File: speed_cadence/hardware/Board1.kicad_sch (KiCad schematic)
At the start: 10 parts, among them IC1 AH1912-W-7, J1 DX07S016JA3R1500, SW1 SW_Push, U1 STM32F042G6U6TR, U2 TS2940CW33_RPG

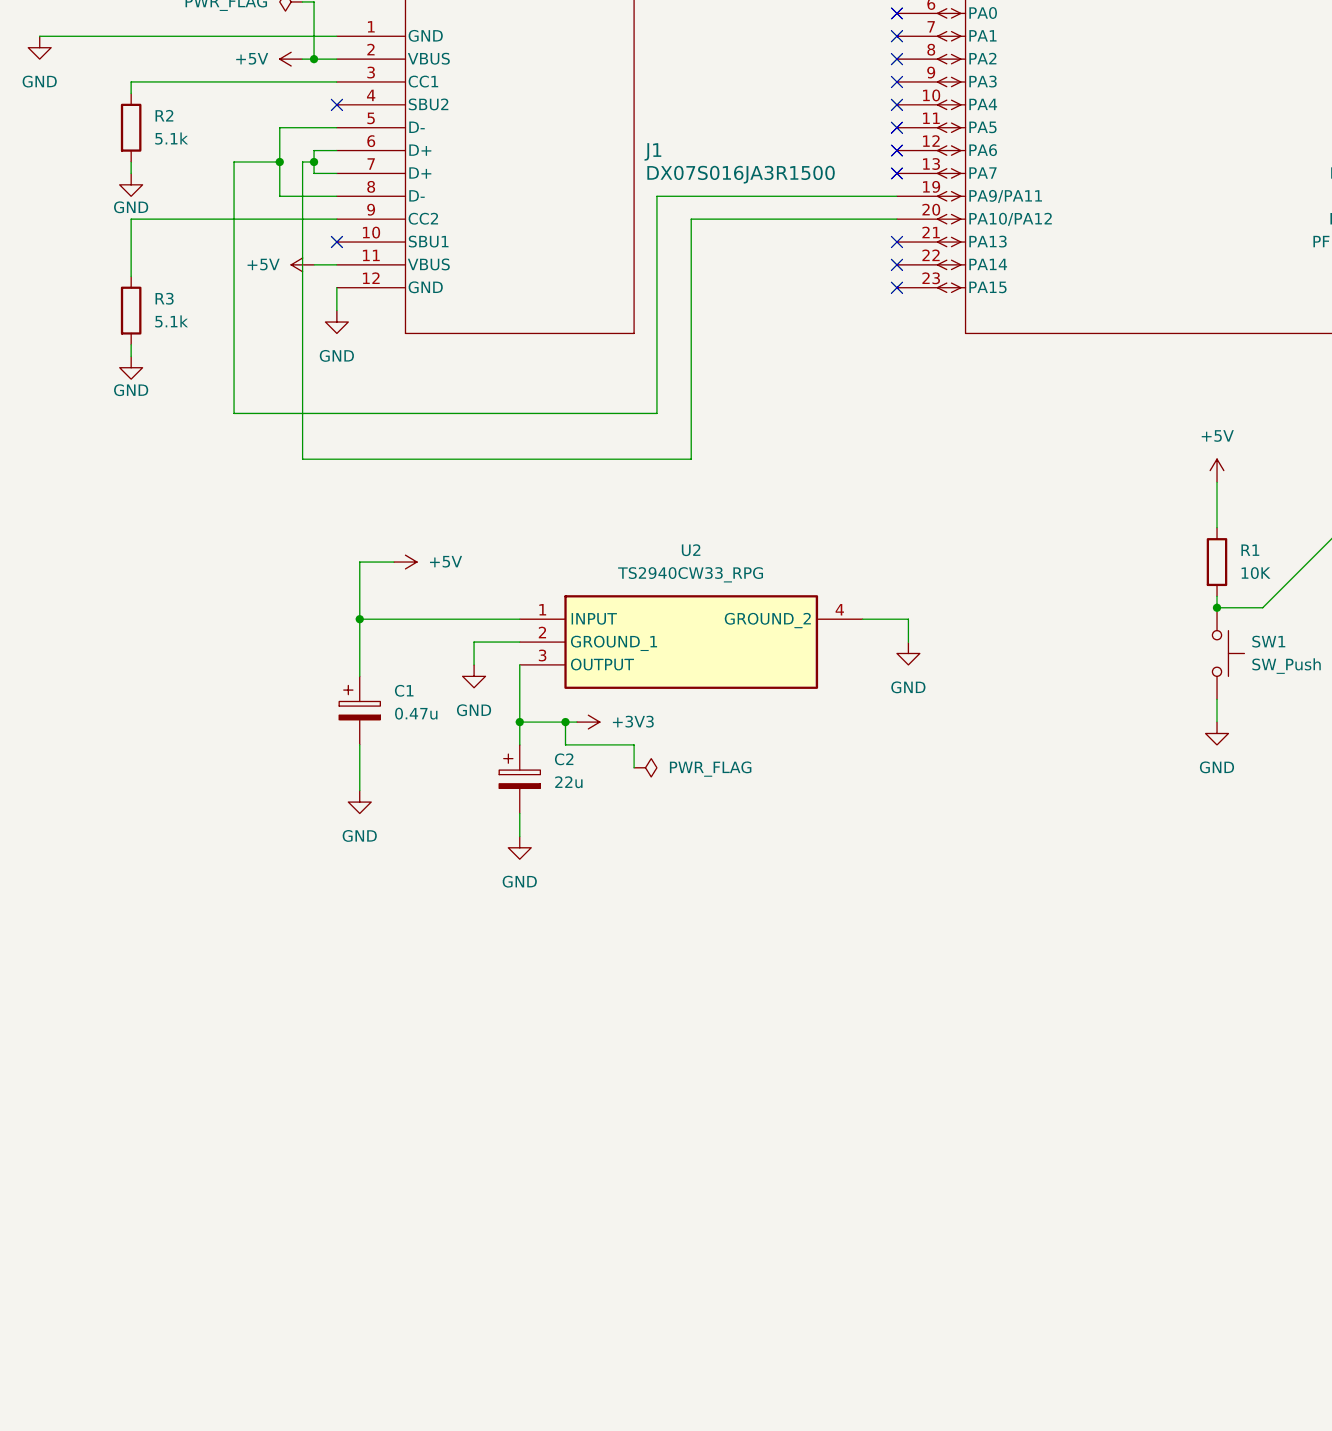
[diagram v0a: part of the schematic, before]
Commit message: Added final pins and finished physical layout
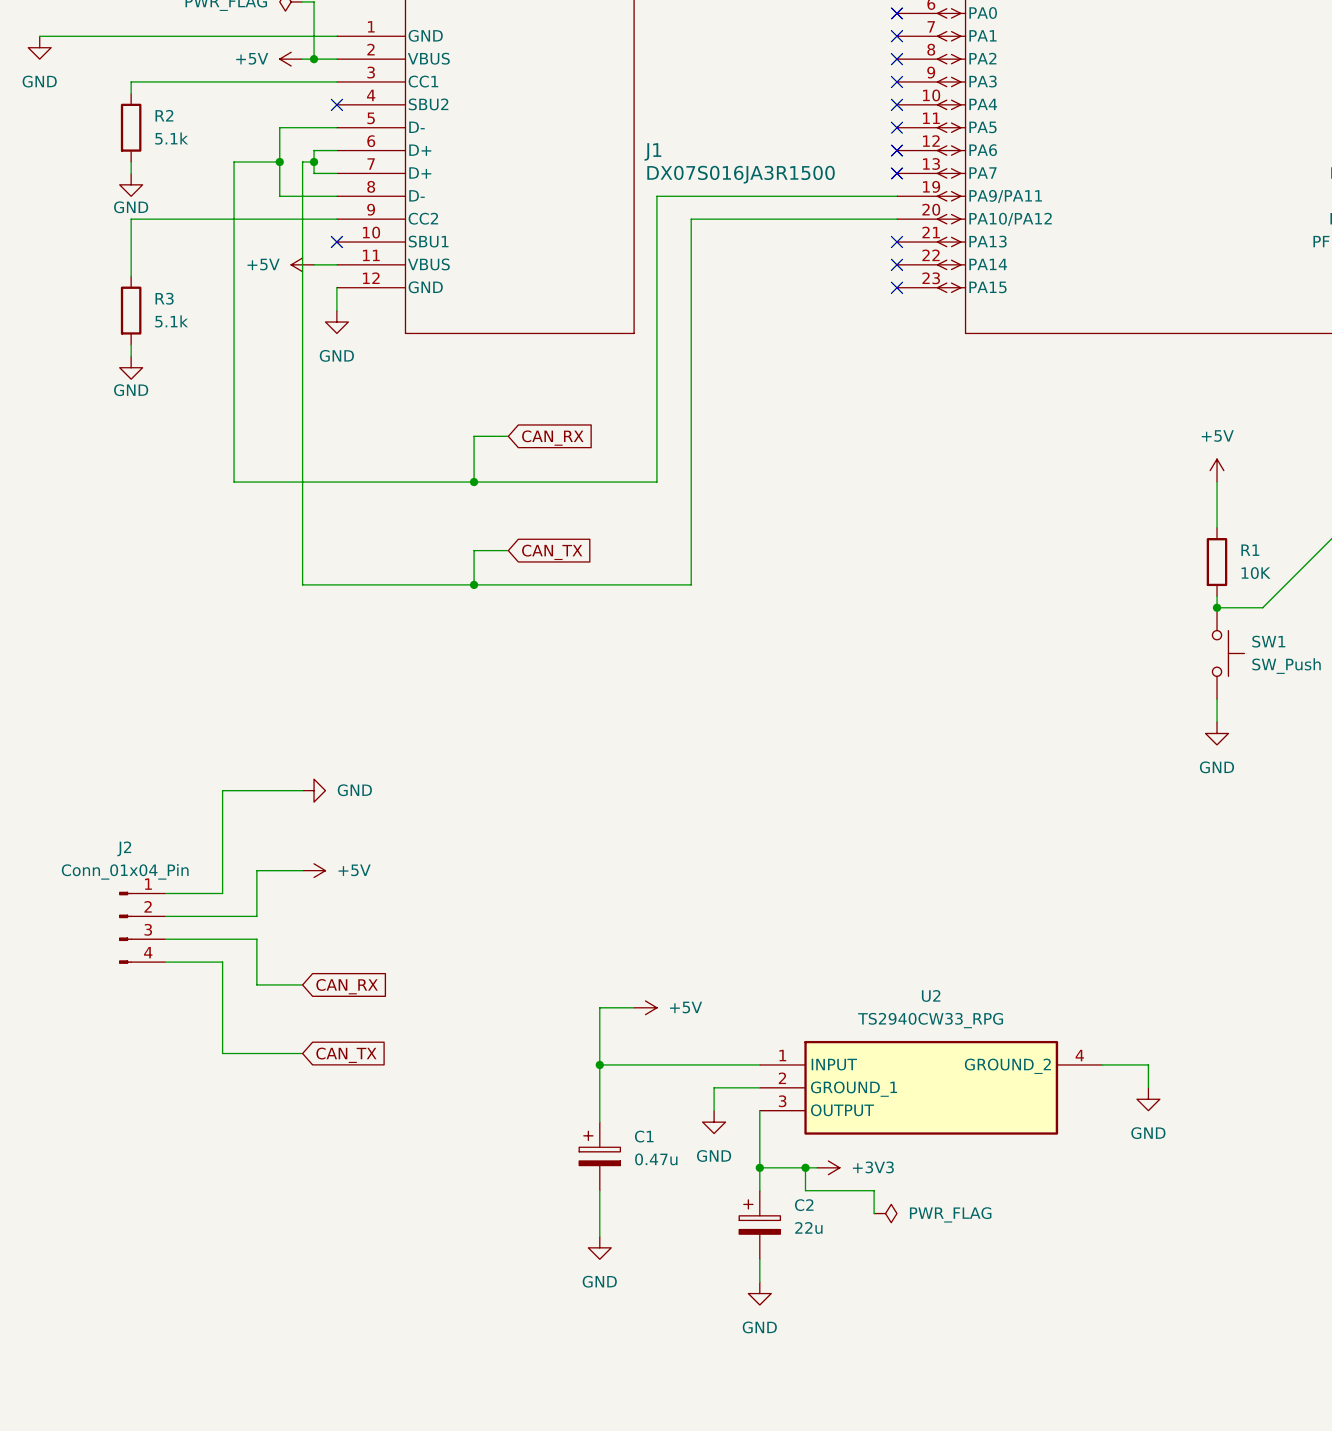
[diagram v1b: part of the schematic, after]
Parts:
- added J2: Conn_01x04_Pin, Connector_PinHeader_2.00mm:PinHeader_1x04_P2.00mm_Vertical, symbol Connector:Conn_01x04_Pin
- J1: footprint DX07S016JA3R1500_USBC:CONN12_DX07S_JAE -> CONN12_DX07S_JAE
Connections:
- net +5V: now also J2.2 (Pin_2)
- net GND: now also J2.1 (Pin_1)
- net CAN_RX: now reaches J1.5 (D-), J1.8 (D-), U1.19 (PA9/PA11)
- net CAN_RX: now also J2.3 (Pin_3)
- net CAN_TX: now reaches J1.6 (D+), J1.7 (D+), U1.20 (PA10/PA12)
- net CAN_TX: now also J2.4 (Pin_4)
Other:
- moved on the sheet: C1, C2, U2

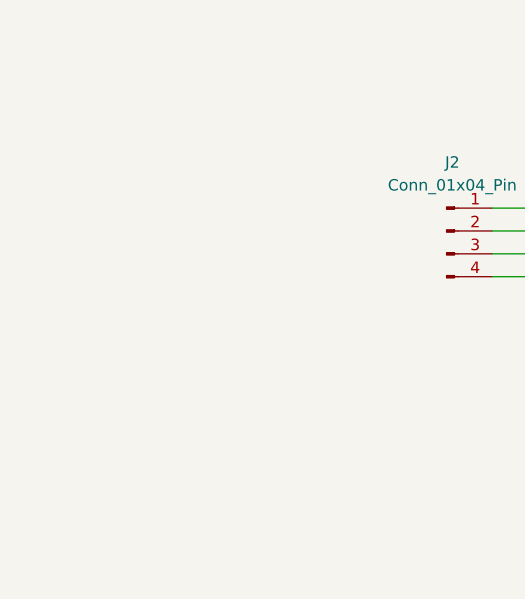
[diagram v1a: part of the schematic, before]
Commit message: Added mounting holes
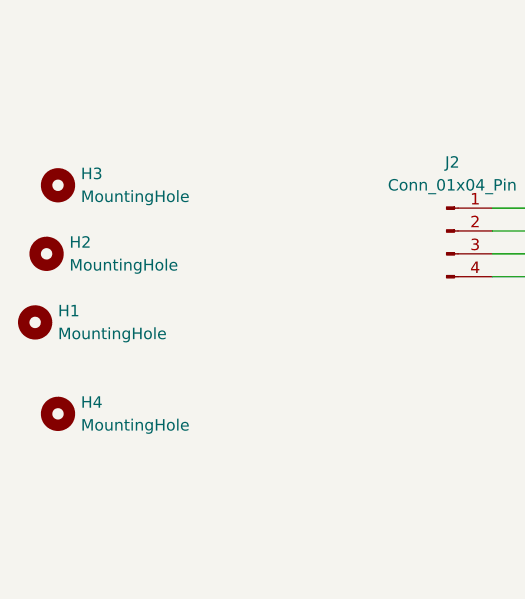
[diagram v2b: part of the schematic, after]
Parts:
- added H1, H2, H3, H4: MountingHole, MountingHole:MountingHole_3.2mm_M3_ISO14580, symbol Mechanical:MountingHole

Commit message: Add files via upload
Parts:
- added J3: Conn_ST_STDC14, Connector_PinHeader_1.27mm:PinHeader_2x07_P1.27mm_Vertical_SMD, symbol Connector:Conn_ST_STDC14
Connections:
- net +3V3: now also J3.3 (VCC)
- net CAN_RX: now also J3.13 (VCP_RX)
- net CAN_TX: now also J3.14 (VCP_TX)
- net GND: now also J3.11 (GNDDetect), J3.5 (GND), J3.7 (GND)
- net RESET_PROG: now reaches R1.2, SW1.1, U1.4 (NRST)
- net RESET_PROG: now also J3.12 (~{RST})
- net codeio: now reaches U1.21 (PA13)
- net codeio: now also J3.4 (JTMS/SWDIO)
- net codeclk: now reaches U1.22 (PA14)
- net codeclk: now also J3.6 (JCLK/SWCLK)
- no-connect marks 24 -> 25
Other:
- note added: "PROGRAMMER CONNECTOR (JTAG)"
- moved on the sheet: U1B

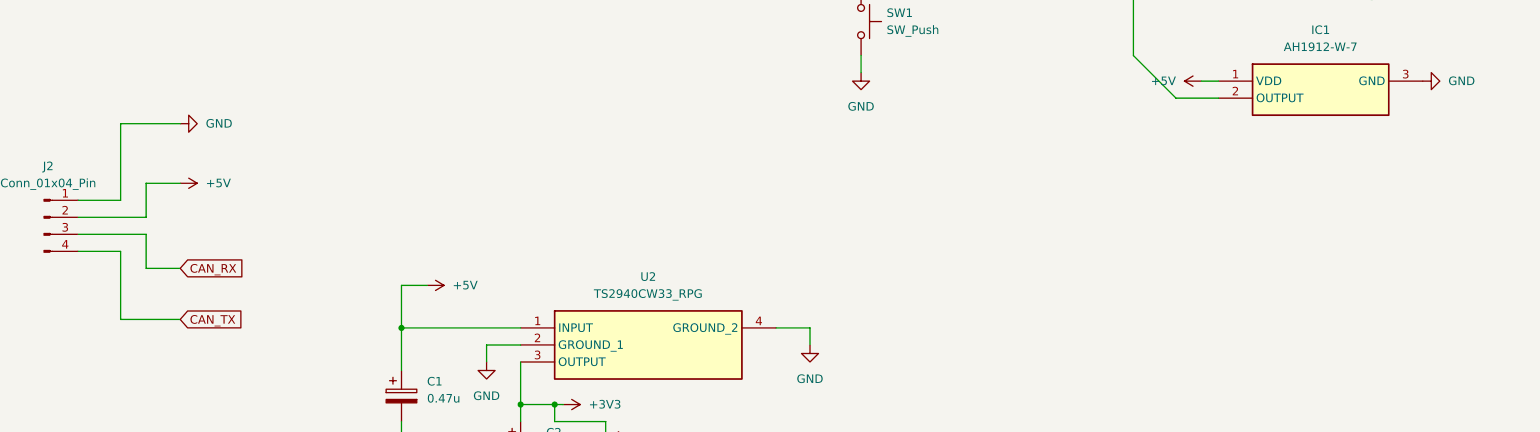
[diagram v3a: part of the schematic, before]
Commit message: Added in connector for "battery" to PCB layout
There are 37 errors to either ignore or fix, but they should all be reviewed.
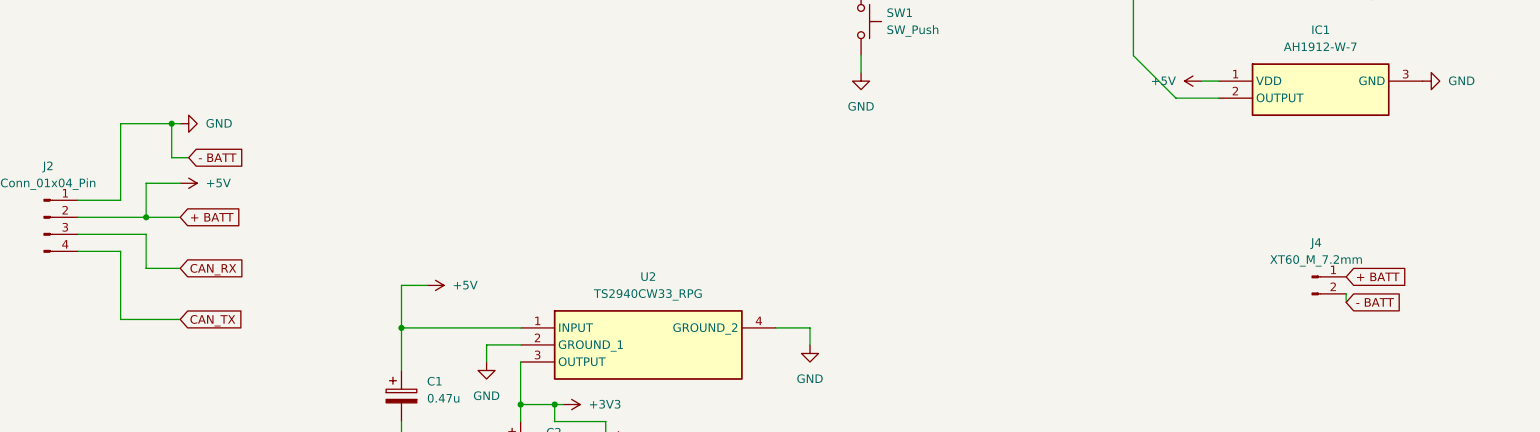
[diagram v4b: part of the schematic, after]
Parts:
- added J4: XT60_M_7.2mm, Connector_AMASS:AMASS_XT60-M_1x02_P7.20mm_Vertical, symbol Connector:Conn_01x02_Pin
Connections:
- net +5V: now also J4.1 (Pin_1)
- net GND: now also J4.2 (Pin_2)
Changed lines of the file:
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@@
 	)
 	(junction
+		(at 46.99 128.27)
+		(diameter 0)
+		(color 0 0 0 0)
+	)
+	(junction
 		(at 149.86 107.95)
 		(diameter 0)
@@
 	)
 	(junction
+		(at 43.18 142.24)
+		(diameter 0)
+		(color 0 0 0 0)
+	)
+	(junction
 		(at 49.53 58.42)
 		(diameter 0)
@@
 	(wire
 		(pts
+			(xy 43.18 142.24) (xy 48.26 142.24)
+		)
+		(stroke
+			(width 0)
+			(type default)
+		)
+	)
+	(wire
+		(pts
 			(xy 111.76 172.72) (xy 104.14 172.72)
 		)
@@
 	(wire
 		(pts
+			(xy 222.25 153.67) (xy 222.25 154.94)
+		)
+		(stroke
+			(width 0)
+			(type default)
+		)
+	)
+	(wire
+		(pts
 			(xy 49.53 40.64) (xy 49.53 46.99)
 		)
@@
 	(wire
 		(pts
+			(xy 46.99 128.27) (xy 48.26 128.27)
+		)
+		(stroke
+			(width 0)
+			(type default)
+		)
+	)
+	(wire
+		(pts
 			(xy 81.28 152.4) (xy 81.28 158.75)
 		)
@@
 	(wire
 		(pts
-			(xy 39.37 128.27) (xy 48.26 128.27)
+			(xy 39.37 128.27) (xy 46.99 128.27)
 		)
 		(stroke
@@
 	(wire
 		(pts
+			(xy 46.99 133.35) (xy 49.53 133.35)
+		)
+		(stroke
+			(width 0)
+			(type default)
+		)
+	)
+	(wire
+		(pts
 			(xy 104.14 172.72) (xy 104.14 170.18)
 		)
@@
 	(wire
 		(pts
+			(xy 46.99 128.27) (xy 46.99 133.35)
+		)
+		(stroke
+			(width 0)
+			(type default)
+		)
+	)
+	(wire
+		(pts
 			(xy 137.16 158.75) (xy 142.24 158.75)
 		)
@@
 		)
 	)
+	(global_label "+ BATT"
+		(shape input)
+		(at 48.26 142.24 0)
+		(fields_autoplaced yes)
+		(effects
+			(font
+				(size 1.27 1.27)
+			)
+			(justify left)
+		)
+		(property "Intersheetrefs" "${INTERSHEET_REFS}"
+			(at 58.079 142.24 0)
+			(effects
+				(font
+					(size 1.27 1.27)
+				)
+				(justify left)
+				(hide yes)
+			)
+		)
+	)
 	(global_label "Prog_RX"
 		(shape input)
@@
 		)
 	)
+	(global_label "- BATT"
+		(shape input)
+		(at 49.53 133.35 0)
+		(fields_autoplaced yes)
+		(effects
+			(font
+				(size 1.27 1.27)
+			)
+			(justify left)
+		)
+		(property "Intersheetrefs" "${INTERSHEET_REFS}"
+			(at 59.349 133.35 0)
+			(effects
+				(font
+					(size 1.27 1.27)
+				)
+				(justify left)
+				(hide yes)
+			)
+		)
+	)
 	(global_label "Prog_RX"
 		(shape input)
@@
 		)
 	)
+	(global_label "+ BATT"
+		(shape input)
+		(at 222.25 151.13 0)
+		(fields_autoplaced yes)
+		(effects
+			(font
+				(size 1.27 1.27)
+			)
+			(justify left)
+		)
+		(property "Intersheetrefs" "${INTERSHEET_REFS}"
+			(at 232.069 151.13 0)
+			(effects
+				(font
+					(size 1.27 1.27)
+				)
+				(justify left)
+				(hide yes)
+			)
+		)
+	)
+	(global_label "- BATT"
+		(shape input)
+		(at 222.25 154.94 0)
+		(fields_autoplaced yes)
+		(effects
+			(font
+				(size 1.27 1.27)
+			)
+			(justify left)
+		)
+		(property "Intersheetrefs" "${INTERSHEET_REFS}"
+			(at 232.069 154.94 0)
+			(effects
+				(font
+					(size 1.27 1.27)
+				)
+				(justify left)
+				(hide yes)
+			)
+		)
+	)
 	(symbol
 		(lib_id "Mechanical:MountingHole")
@@
 				)
 			)
+		)
+	)
+	(symbol
+		(lib_id "Connector:Conn_01x02_Pin")
+		(at 217.17 151.13 0)
+		(unit 1)
+		(exclude_from_sim no)
+		(in_bom yes)
+		(on_board yes)
+		(dnp no)
+		(fields_autoplaced yes)
+		(property "Reference" "J4"
+			(at 217.805 146.05 0)
+			(effects
+				(font
+					(size 1.27 1.27)
+				)
+			)
+		)
+		(property "Value" "XT60_M_7.2mm"
+			(at 217.805 148.59 0)
+			(effects
+				(font
+					(size 1.27 1.27)
+				)
+			)
+		)
+		(property "Footprint" "Connector_AMASS:AMASS_XT60-M_1x02_P7.20mm_Vertical"
+			(at 217.17 151.13 0)
+			(effects
+				(font
+					(size 1.27 1.27)
+				)
+				(hide yes)
+			)
+		)
+		(property "Datasheet" "~"
+			(at 217.17 151.13 0)
+			(effects
+				(font
+					(size 1.27 1.27)
+				)
+				(hide yes)
+			)
+		)
+		(property "Description" "Generic connector, single row, 01x02, script generated"
+			(at 217.17 151.13 0)
+			(effects
+				(font
+					(size 1.27 1.27)
+				)
+				(hide yes)
+			)
+		)
+		(pin "2"
+		)
+		(pin "1"
+		)
+		(instances
+			(project "Board1"
+				(path "/10163266-8018-4064-a980-f3c4e9dfe9d4"
+					(reference "J4")
+					(unit 1)
+				)
+			)

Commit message: Orientation
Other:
- note added: "5V to 3V3"
- note added: "USB-C Port"
- moved on the sheet: C1, C2, H1, H2, H4, IC1, J3, R1, SW1, U1B, U2
